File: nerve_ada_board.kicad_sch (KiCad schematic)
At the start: 64 parts, among them J10 CAN1, J11 CAN2, J2 TC2050-IDC, J3 2171750001, J5 WS2812B, J6 Camera, J7 PA4-7, J8 PC1-3, J9 PB4-5, SW1 SPST, SW2 SPST, SW3 SPST, U1 LD1117S33TR_SOT223, U2 STM32F446RET, U3 SAM-M10Q, U4 XBP9B-DMWT-002, U8 TXB0104QPWRQ1, U9 TXB0104QPWRQ1, Y1 8M, Y2 32k768

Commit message: Resolve ERC duplicate labelling warning
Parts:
- renumbered J8 to J10, J9 to J11, J10 to J7, J11 to J8, J7 to J9
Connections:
- net CAN1_HIGH+ renamed CAN1+
- net CAN1_LOW- renamed CAN1-
- net CAN2_HIGH+ renamed CAN2+
- net CAN2_LOW- renamed CAN2-
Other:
- moved on the sheet: J7, J8
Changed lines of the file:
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@@
 	(wire
 		(pts
-			(xy 262.89 163.83) (xy 271.78 163.83)
-		)
-		(stroke
-			(width 0)
-			(type default)
-		)
-	)
-	(wire
-		(pts
 			(xy 135.89 57.15) (xy 135.89 58.42)
 		)
@@
 	(wire
 		(pts
-			(xy 262.89 161.29) (xy 271.78 161.29)
-		)
-		(stroke
-			(width 0)
-			(type default)
-		)
-	)
-	(wire
-		(pts
 			(xy 167.64 121.92) (xy 167.64 123.19)
 		)
@@
 	(wire
 		(pts
-			(xy 205.74 161.29) (xy 214.63 161.29)
-		)
-		(stroke
-			(width 0)
-			(type default)
-		)
-	)
-	(wire
-		(pts
 			(xy 118.11 180.34) (xy 119.38 180.34)
 		)
@@
 	(wire
 		(pts
-			(xy 205.74 163.83) (xy 214.63 163.83)
-		)
-		(stroke
-			(width 0)
-			(type default)
-		)
-	)
-	(wire
-		(pts
 			(xy 85.09 180.34) (xy 86.36 180.34)
 		)
@@
 		)
 	)
-	(label "CAN2+"
-		(at 264.16 161.29 0)
-		(fields_autoplaced yes)
-		(effects
-			(font
-				(size 1.27 1.27)
-			)
-			(justify left bottom)
-		)
-	)
 	(label "LSE_OUT"
 		(at 58.42 118.11 180)
@@
 	)
 	(label "CAN1+"
-		(at 207.01 161.29 0)
-		(fields_autoplaced yes)
-		(effects
-			(font
-				(size 1.27 1.27)
-			)
-			(justify left bottom)
-		)
-	)
-	(label "CAN1+"
 		(at 205.74 152.4 0)
 		(fields_autoplaced yes)
@@
 		)
 	)
-	(label "CAN2-"
-		(at 264.16 163.83 0)
-		(fields_autoplaced yes)
-		(effects
-			(font
-				(size 1.27 1.27)
-			)
-			(justify left bottom)
-		)
-	)
-	(label "CAN1-"
-		(at 207.01 163.83 0)
-		(fields_autoplaced yes)
-		(effects
-			(font
-				(size 1.27 1.27)
-			)
-			(justify left bottom)
-		)
-	)
 	(hierarchical_label "SWO"
 		(shape input)
@@
 		)
 	)
-	(hierarchical_label "CAN1_LOW-"
-		(shape input)
-		(at 213.36 154.94 0)
-		(fields_autoplaced yes)
-		(effects
-			(font
-				(size 1.27 1.27)
-			)
-			(justify left)
-		)
-	)
 	(hierarchical_label "GPIO_IMU_P0"
 		(shape input)
@@
 		)
 	)
-	(hierarchical_label "CAN1_HIGH+"
-		(shape input)
-		(at 205.74 161.29 180)
-		(fields_autoplaced yes)
-		(effects
-			(font
-				(size 1.27 1.27)
-			)
-			(justify right)
-		)
-	)
 	(hierarchical_label "CAN2_RX"
 		(shape input)
@@
 		)
 	)
-	(hierarchical_label "CAN1_LOW-"
-		(shape input)
-		(at 205.74 163.83 180)
-		(fields_autoplaced yes)
-		(effects
-			(font
-				(size 1.27 1.27)
-			)
-			(justify right)
-		)
-	)
 	(hierarchical_label "PB5_EXP"
 		(shape input)
@@
 		)
 	)
-	(hierarchical_label "CAN2_HIGH+"
-		(shape input)
-		(at 270.51 152.4 0)
-		(fields_autoplaced yes)
-		(effects
-			(font
-				(size 1.27 1.27)
-			)
-			(justify left)
-		)
-	)
 	(hierarchical_label "PC2"
 		(shape input)
@@
 		)
 	)
-	(hierarchical_label "CAN1_HIGH+"
-		(shape input)
-		(at 213.36 152.4 0)
-		(fields_autoplaced yes)
-		(effects
-			(font
-				(size 1.27 1.27)
-			)
-			(justify left)
-		)
-	)
 	(hierarchical_label "USART2_RX"
 		(shape input)
@@
 		)
 	)
-	(hierarchical_label "CAN2_LOW-"
-		(shape input)
-		(at 270.51 154.94 0)
-		(fields_autoplaced yes)
-		(effects
-			(font
-				(size 1.27 1.27)
-			)
-			(justify left)
-		)
-	)
 	(hierarchical_label "GPIO_SPI2_CS"
 		(shape input)
@@
 		)
 	)
-	(hierarchical_label "CAN2_HIGH+"
-		(shape input)
-		(at 262.89 161.29 180)
-		(fields_autoplaced yes)
-		(effects
-			(font
-				(size 1.27 1.27)
-			)
-			(justify right)
-		)
-	)
 	(hierarchical_label "SDIO_DET"
 		(shape input)
@@
 		)
 	)
-	(hierarchical_label "CAN2_LOW-"
-		(shape input)
-		(at 262.89 163.83 180)
-		(fields_autoplaced yes)
-		(effects
-			(font
-				(size 1.27 1.27)
-			)
-			(justify right)
-		)
-	)
 	(hierarchical_label "CAN1_TX"
 		(shape input)
@@
 	(symbol
 		(lib_id "Connector:Conn_01x02_Pin")
-		(at 276.86 161.29 0)
+		(at 275.59 152.4 0)
 		(mirror y)
 		(unit 1)
@@
 		(on_board yes)
 		(dnp no)
-		(property "Reference" "J11"
-			(at 277.876 161.29 0)
+		(property "Reference" "J8"
+			(at 276.606 152.4 0)
 			(effects
 				(font
@@
 		)
 		(property "Value" "CAN2"
-			(at 277.876 163.83 0)
+			(at 276.606 154.94 0)
 			(effects
 				(font
@@
 		)
 		(property "Footprint" "Connector_PinHeader_2.54mm:PinHeader_1x02_P2.54mm_Vertical"
-			(at 276.86 161.29 0)
+			(at 275.59 152.4 0)
 			(effects
 				(font
@@
 		)
 		(property "Datasheet" "~"
-			(at 276.86 161.29 0)
+			(at 275.59 152.4 0)
 			(effects
 				(font
@@
 		)
 		(property "Description" "Generic connector, single row, 01x02, script generated"
-			(at 276.86 161.29 0)
+			(at 275.59 152.4 0)
 			(effects
 				(font
@@
 			(project ""
 				(path "/c0277862-b3f2-4e0e-986f-34702f0543f0"
-					(reference "J11")
+					(reference "J8")
 					(unit 1)
 				)
@@
 		(dnp no)
 		(fields_autoplaced yes)
-		(property "Reference" "J8"
+		(property "Reference" "J10"
 			(at 67.31 154.9399 0)
 			(effects
@@
 			(project ""
 				(path "/c0277862-b3f2-4e0e-986f-34702f0543f0"
-					(reference "J8")
+					(reference "J10")
 					(unit 1)
 				)
@@
 		(on_board yes)
 		(dnp no)
-		(property "Reference" "J7"
+		(property "Reference" "J9"
 			(at 28.956 154.686 0)
 			(effects
@@
 			(project "nerve_ada_board"
 				(path "/c0277862-b3f2-4e0e-986f-34702f0543f0"
-					(reference "J7")
+					(reference "J9")
 					(unit 1)
 				)
@@
 	(symbol
 		(lib_id "Connector:Conn_01x02_Pin")
-		(at 219.71 161.29 0)
+		(at 218.44 152.4 0)
 		(mirror y)
 		(unit 1)
@@
 		(on_board yes)
 		(dnp no)
-		(property "Reference" "J10"
-			(at 220.726 161.29 0)
+		(property "Reference" "J7"
+			(at 219.456 152.4 0)
 			(effects
 				(font
@@
 		)
 		(property "Value" "CAN1"
-			(at 220.726 163.83 0)
+			(at 219.456 154.94 0)
 			(effects
 				(font
@@
 		)
 		(property "Footprint" "Connector_PinHeader_2.54mm:PinHeader_1x02_P2.54mm_Vertical"
-			(at 219.71 161.29 0)
+			(at 218.44 152.4 0)
 			(effects
 				(font
@@
 		)
 		(property "Datasheet" "~"
-			(at 219.71 161.29 0)
+			(at 218.44 152.4 0)
 			(effects
 				(font
@@
 		)
 		(property "Description" "Generic connector, single row, 01x02, script generated"
-			(at 219.71 161.29 0)
+			(at 218.44 152.4 0)
 			(effects
 				(font
@@
 			(project "nerve_ada_board"
 				(path "/c0277862-b3f2-4e0e-986f-34702f0543f0"
-					(reference "J10")
+					(reference "J7")
 					(unit 1)
 				)
@@
 		(on_board yes)
 		(dnp no)
-		(property "Reference" "J9"
+		(property "Reference" "J11"
 			(at 96.52 156.21 0)
 			(effects
@@
 			(project "nerve_ada_board"
 				(path "/c0277862-b3f2-4e0e-986f-34702f0543f0"
-					(reference "J9")
+					(reference "J11")
 					(unit 1)
 				)

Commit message: Flight ready alpha and update components
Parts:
- removed J1: ~, adafruit:adafruit_4682_sdio_card, symbol adafruit:adafruit_4682_sdio_card
- removed J12, J13, J14, J15, J16, J17, J18: ~, common:harwin_2p_2-54_jumper_closed, symbol common:harwin_2p_2-54_jumper_closed
- removed J5: WS2812B, Connector_PinHeader_2.54mm:PinHeader_1x03_P2.54mm_Vertical, symbol Connector:Conn_01x03_Pin
- added J1: ~, common:harwin_2p_2-54_jumper_open, symbol common:harwin_2p_2-54_jumper_open
- added J3: 472192001, common:molex_472192001_microsd_hinge, symbol common:molex_472192001_microsd_hinge
- added J6: WS2812B, Connector_PinHeader_2.54mm:PinHeader_1x02_P2.54mm_Vertical, symbol Connector:Conn_01x02_Pin
- added R1, R2, R3, R4, R5: 47k, Resistor_SMD:R_0603_1608Metric, symbol Device:R
- added R6: 10k, Resistor_SMD:R_0603_1608Metric, symbol Device:R
- renumbered J6 to J12, J3 to J4, J4 to J5, R4 to R10, R5 to R11, R6 to R12, R7 to R13, R8 to R14, R1 to R7, R2 to R8, R3 to R9, U9 to U10, U10 to U3, U3 to U4, U4 to U5, U5 to U6, U6 to U7, U7 to U8, U8 to U9
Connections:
- net +3V3: now also J1.1, J3.4 (VDD), R1.1, R2.1, R3.1, R4.1, R5.1
- net GND: now also J3.6 (VSS), J3.G1 (GND), J3.G2 (GND), J3.G3 (GND), J3.G4 (GND), J6.1 (Pin_1), R6.2
- net PB4: now also U9.4 (A3)
- net PB5: now also U9.5 (A4)
- net PC1: now also U10.2 (A1)
- net PC2: now also U10.3 (A2)
- net PC3: now also U10.4 (A3)
- net SDIO_CLK: now also J3.5 (CLK)
- net SDIO_CMD: now also J3.3 (CMD), R3.2
- net SDIO_D0: now also J3.7 (DAT0), R2.2
- net SDIO_D1: now also J3.8 (DAT1), R1.2
- net SDIO_D2: now also J3.1 (DAT2), R5.2
- net SDIO_D3: now also J3.2 (DAT3/CD), R4.2
- net SDIO_DET: now also J1.2, R6.1
- net USART3_RX: now also U9.2 (A1)
- net USART3_TX: now also U9.3 (A2)
- net at D4.2 (DOUT): now also J6.2 (Pin_2)
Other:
- note added: "Manual card detect jumper."
- moved on the sheet: BT1, C6, C7, D1, D2, D3, D4, J10, J11, J12, J7, J8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

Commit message: Fix SDIO card detect for active low
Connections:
- net +3V3: now also R6.1; no longer J1.1
- net GND: now also J1.2; no longer R6.2
- net SDIO_DET: now also J1.1, R6.2; no longer J1.2, R6.1
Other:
- moved on the sheet: J1
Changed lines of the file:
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@@
 	)
 	(junction
-		(at 154.94 24.13)
+		(at 252.73 19.05)
 		(diameter 0)
 		(color 0 0 0 0)
 	)
 	(junction
-		(at 252.73 19.05)
+		(at 181.61 85.09)
 		(diameter 0)
 		(color 0 0 0 0)
 	)
 	(junction
-		(at 181.61 85.09)
+		(at 142.24 27.94)
 		(diameter 0)
 		(color 0 0 0 0)
@@
 	(wire
 		(pts
-			(xy 154.94 21.59) (xy 153.67 21.59)
-		)
-		(stroke
-			(width 0)
-			(type default)
-		)
-	)
-	(wire
-		(pts
 			(xy 93.98 118.11) (xy 95.25 118.11)
 		)
@@
 	(wire
 		(pts
-			(xy 154.94 24.13) (xy 153.67 24.13)
+			(xy 153.67 35.56) (xy 154.94 35.56)
 		)
 		(stroke
@@
 	(wire
 		(pts
-			(xy 154.94 25.4) (xy 154.94 24.13)
-		)
-		(stroke
-			(width 0)
-			(type default)
-		)
-	)
-	(wire
-		(pts
 			(xy 245.11 64.77) (xy 245.11 80.01)
 		)
@@
 	(wire
 		(pts
-			(xy 154.94 24.13) (xy 154.94 21.59)
-		)
-		(stroke
-			(width 0)
-			(type default)
-		)
-	)
-	(wire
-		(pts
 			(xy 171.45 121.92) (xy 171.45 123.19)
 		)
@@
 	(wire
 		(pts
+			(xy 142.24 19.05) (xy 142.24 17.78)
+		)
+		(stroke
+			(width 0)
+			(type default)
+		)
+	)
+	(wire
+		(pts
 			(xy 73.66 34.29) (xy 73.66 50.8)
 		)
@@
 	(wire
 		(pts
+			(xy 142.24 27.94) (xy 142.24 26.67)
+		)
+		(stroke
+			(width 0)
+			(type default)
+		)
+	)
+	(wire
+		(pts
 			(xy 31.75 102.87) (xy 31.75 104.14)
 		)
@@
 	(wire
 		(pts
-			(xy 142.24 21.59) (xy 142.24 17.78)
+			(xy 142.24 35.56) (xy 142.24 27.94)
 		)
 		(stroke
@@
 	(wire
 		(pts
-			(xy 154.94 33.02) (xy 154.94 34.29)
+			(xy 144.78 27.94) (xy 142.24 27.94)
+		)
+		(stroke
+			(width 0)
+			(type default)
+		)
+	)
+	(wire
+		(pts
+			(xy 154.94 35.56) (xy 154.94 36.83)
 		)
 		(stroke
@@
 	(wire
 		(pts
-			(xy 143.51 21.59) (xy 142.24 21.59)
+			(xy 143.51 35.56) (xy 142.24 35.56)
 		)
 		(stroke
@@
 		)
 	)
+	(hierarchical_label "SDIO_DET"
+		(shape input)
+		(at 144.78 27.94 0)
+		(fields_autoplaced yes)
+		(effects
+			(font
+				(size 1.27 1.27)
+			)
+			(justify left)
+		)
+	)
 	(hierarchical_label "USART1_RTS"
 		(shape input)
@@
 		)
 	)
-	(hierarchical_label "SDIO_DET"
-		(shape input)
-		(at 153.67 24.13 180)
-		(fields_autoplaced yes)
-		(effects
-			(font
-				(size 1.27 1.27)
-			)
-			(justify right)
-		)
-	)
 	(hierarchical_label "PC1_EXP"
 		(shape input)
@@
 	)
 	(symbol
+		(lib_id "Device:R")
+		(at 142.24 22.86 0)
+		(unit 1)
+		(exclude_from_sim no)
+		(in_bom yes)
+		(on_board yes)
+		(dnp no)
+		(property "Reference" "R6"
+			(at 138.176 21.59 0)
+			(effects
+				(font
+					(size 1.27 1.27)
+				)
+				(justify left)
+			)
+		)
+		(property "Value" "10k"
+			(at 137.16 24.13 0)
+			(effects
+				(font
+					(size 1.27 1.27)
+				)
+				(justify left)
+			)
+		)
+		(property "Footprint" "Resistor_SMD:R_0603_1608Metric"
+			(at 140.462 22.86 90)
+			(effects
+				(font
+					(size 1.27 1.27)
+				)
+				(hide yes)
+			)
+		)
+		(property "Datasheet" "~"
+			(at 142.24 22.86 0)
+			(effects
+				(font
+					(size 1.27 1.27)
+				)
+				(hide yes)
+			)
+		)
+		(property "Description" "Resistor"
+			(at 142.24 22.86 0)
+			(effects
+				(font
+					(size 1.27 1.27)
+				)
+				(hide yes)
+			)
+		)
+		(pin "2"
+		)
+		(pin "1"
+		)
+		(instances
+			(project "nerve_ada_board"
+				(path "/c0277862-b3f2-4e0e-986f-34702f0543f0"
+					(reference "R6")
+					(unit 1)
+				)
+			)
+		)
+	)
+	(symbol
 		(lib_id "power:GND")
-		(at 154.94 34.29 0)
+		(at 154.94 36.83 0)
 		(unit 1)
 		(exclude_from_sim no)
@@
 		(fields_autoplaced yes)
 		(property "Reference" "#PWR010"
-			(at 154.94 40.64 0)
+			(at 154.94 43.18 0)
 			(effects
 				(font
@@
 		)
 		(property "Value" "GND"
-			(at 154.94 39.37 0)
+			(at 154.94 41.91 0)
 			(effects
 				(font
@@
 		)
 		(property "Footprint" ""
-			(at 154.94 34.29 0)
+			(at 154.94 36.83 0)
 			(effects
 				(font
@@
 		)
 		(property "Datasheet" ""
-			(at 154.94 34.29 0)
+			(at 154.94 36.83 0)
 			(effects
 				(font
@@
 		)
 		(property "Description" "Power symbol creates a global label with name \"GND\" , ground"
-			(at 154.94 34.29 0)
+			(at 154.94 36.83 0)
 			(effects
 				(font
@@
 	)
 	(symbol
-		(lib_id "Device:R")
-		(at 154.94 29.21 0)
-		(unit 1)
-		(exclude_from_sim no)
-		(in_bom yes)
-		(on_board yes)
-		(dnp no)
-		(property "Reference" "R6"
-			(at 150.876 27.94 0)
-			(effects
-				(font
-					(size 1.27 1.27)
-				)
-				(justify left)
-			)
-		)
-		(property "Value" "10k"
-			(at 149.86 30.48 0)
-			(effects
-				(font
-					(size 1.27 1.27)
-				)
-				(justify left)
-			)
-		)
-		(property "Footprint" "Resistor_SMD:R_0603_1608Metric"
-			(at 153.162 29.21 90)
-			(effects
-				(font
-					(size 1.27 1.27)
-				)
-				(hide yes)
-			)
-		)
-		(property "Datasheet" "~"
-			(at 154.94 29.21 0)
-			(effects
-				(font
-					(size 1.27 1.27)
-				)
-				(hide yes)
-			)
-		)
-		(property "Description" "Resistor"
-			(at 154.94 29.21 0)
-			(effects
-				(font
-					(size 1.27 1.27)
-				)
-				(hide yes)
-			)
-		)
-		(pin "2"
-		)
-		(pin "1"
-		)
-		(instances
-			(project "nerve_ada_board"
-				(path "/c0277862-b3f2-4e0e-986f-34702f0543f0"
-					(reference "R6")
-					(unit 1)
-				)
-			)
-		)
-	)
-	(symbol
 		(lib_id "power:+3V3")
 		(at 16.51 17.78 0)
@@
 	(symbol
 		(lib_id "common:harwin_2p_2-54_jumper_open")
-		(at 148.59 21.59 0)
+		(at 148.59 35.56 0)
 		(unit 1)
 		(exclude_from_sim no)
@@
 		(dnp no)
 		(property "Reference" "J1"
-			(at 148.59 18.288 0)
+			(at 148.59 32.258 0)
 			(effects
 				(font
@@
 		)
 		(property "Value" "~"
-			(at 148.59 17.78 0)
+			(at 148.59 31.75 0)
 			(effects
 				(font
@@
 		)
 		(property "Footprint" "common:harwin_2p_2-54_jumper_open"
-			(at 152.4 27.94 0)
+			(at 152.4 41.91 0)
 			(effects
 				(font
@@
 		)
 		(property "Datasheet" "https://cdn.harwin.com/pdfs/M20-999.pdf"
-			(at 184.15 29.083 0)
+			(at 184.15 43.053 0)
 			(effects
 				(font
@@
 		)
 		(property "Description" "Connector Header Through Hole 2 position 0.100\" (2.54mm)"
-			(at 184.15 29.083 0)
+			(at 184.15 43.053 0)
 			(effects
 				(font
@@
 		)
 		(property "Manufacturer" "Harwin"
-			(at 184.15 20.193 0)
+			(at 184.15 34.163 0)
 			(effects
 				(font
@@
 		)
 		(property "Manufacturer Part Number" "M20-9990246"
-			(at 184.15 20.193 0)
+			(at 184.15 34.163 0)
 			(effects
 				(font
@@
 		)
 		(property "Distributor" "DigiKey"
-			(at 184.15 20.193 0)
+			(at 184.15 34.163 0)
 			(effects
 				(font
@@
 		)
 		(property "Distributor Part Number" "952-2262-ND"
-			(at 184.15 29.083 0)
+			(at 184.15 43.053 0)
 			(effects
 				(font
@@
 		)
 		(property "Distributor Link" "https://www.digikey.ca/en/products/detail/harwin-inc/M20-9990246/3728226"
-			(at 184.15 29.083 0)
+			(at 184.15 43.053 0)
 			(effects
 				(font

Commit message: Swap to LD39150DT33-R regulator
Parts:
- removed U1: LD1117S33TR_SOT223, Package_TO_SOT_SMD:SOT-223-3_TabPin2, symbol Regulator_Linear:LD1117S33TR_SOT223
- added U1: ld39150dt33-r, common:to-252-2_dpak-2-leg, symbol common:ld39150dt33-r
- C8: value 100n -> 1u
- C9: value 10u -> 2u2; footprint Capacitor_SMD:C_0805_2012Metric -> Capacitor_SMD:C_0603_1608Metric
- renumbered J2 to J1, J3 to J2, J4 to J3, J1 to J4
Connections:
- net +3V3: now also U1.3 (VO)
- net +5V: now also U1.1 (VI)
- net GND: now also U1.2 (GND)
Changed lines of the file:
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@@
 			)
 		)
-		(property "Value" "10u"
+		(property "Value" "2u2"
 			(at 280.67 31.75 0)
 			(effects
@@
 			)
 		)
-		(property "Footprint" "Capacitor_SMD:C_0805_2012Metric"
+		(property "Footprint" "Capacitor_SMD:C_0603_1608Metric"
 			(at 279.0952 34.29 0)
 			(effects
@@
 			)
 		)
-		(property "Value" "100n"
+		(property "Value" "1u"
 			(at 255.27 31.75 0)
 			(effects
@@
 		(on_board yes)
 		(dnp no)
-		(property "Reference" "J3"
+		(property "Reference" "J2"
 			(at 194.056 45.974 0)
 			(effects
@@
 			(project ""
 				(path "/c0277862-b3f2-4e0e-986f-34702f0543f0"
-					(reference "J3")
+					(reference "J2")
 					(unit 1)
 				)
@@
 	)
 	(symbol
-		(lib_id "Regulator_Linear:LD1117S33TR_SOT223")
-		(at 265.43 25.4 0)
-		(unit 1)
-		(exclude_from_sim no)
-		(in_bom yes)
-		(on_board yes)
-		(dnp no)
-		(property "Reference" "U1"
-			(at 265.43 19.304 0)
-			(effects
-				(font
-					(size 1.27 1.27)
-				)
-			)
-		)
-		(property "Value" "LD1117S33TR_SOT223"
-			(at 265.43 21.844 0)
-			(effects
-				(font
-					(size 1.27 1.27)
-				)
-			)
-		)
-		(property "Footprint" "Package_TO_SOT_SMD:SOT-223-3_TabPin2"
-			(at 265.43 20.32 0)
-			(effects
-				(font
-					(size 1.27 1.27)
-				)
-				(hide yes)
-			)
-		)
-		(property "Datasheet" "http://www.st.com/st-web-ui/static/active/en/resource/technical/document/datasheet/CD00000544.pdf"
-			(at 267.97 31.75 0)
-			(effects
-				(font
-					(size 1.27 1.27)
-				)
-				(hide yes)
-			)
-		)
-		(property "Description" "800mA Fixed Low Drop Positive Voltage Regulator, Fixed Output 3.3V, SOT-223"
-			(at 265.43 25.4 0)
-			(effects
-				(font
-					(size 1.27 1.27)
-				)
-				(hide yes)
-			)
-		)
-		(pin "2"
-		)
-		(pin "3"
-		)
-		(pin "1"
-		)
-		(instances
-			(project ""
-				(path "/c0277862-b3f2-4e0e-986f-34702f0543f0"
-					(reference "U1")
-					(unit 1)
-				)
-			)
-		)
-	)
-	(symbol
 		(lib_id "Device:R")
 		(at 107.95 48.26 0)
@@
 		(on_board yes)
 		(dnp no)
-		(property "Reference" "J4"
+		(property "Reference" "J3"
 			(at 231.14 16.256 0)
 			(effects
@@
 			(project ""
 				(path "/c0277862-b3f2-4e0e-986f-34702f0543f0"
-					(reference "J4")
+					(reference "J3")
 					(unit 1)
 				)
@@
 		(dnp no)
 		(fields_autoplaced yes)
-		(property "Reference" "#PWR010"
+		(property "Reference" "#PWR011"
 			(at 154.94 43.18 0)
 			(effects
@@
 			(project "nerve_ada_board"
 				(path "/c0277862-b3f2-4e0e-986f-34702f0543f0"
-					(reference "#PWR010")
+					(reference "#PWR011")
 					(unit 1)
 				)
@@
 		(dnp no)
 		(fields_autoplaced yes)
-		(property "Reference" "#PWR011"
+		(property "Reference" "#PWR010"
 			(at 129.54 43.18 0)
 			(effects
@@
 			(project "nerve_ada_board"
 				(path "/c0277862-b3f2-4e0e-986f-34702f0543f0"
-					(reference "#PWR011")
+					(reference "#PWR010")
 					(unit 1)
 				)
@@
 		(on_board yes)
 		(dnp no)
-		(property "Reference" "J1"
+		(property "Reference" "J4"
 			(at 148.59 32.258 0)
 			(effects
@@
 			(project "nerve_ada_board"
 				(path "/c0277862-b3f2-4e0e-986f-34702f0543f0"
-					(reference "J1")
+					(reference "J4")
 					(unit 1)
 				)
@@
 		(on_board yes)
 		(dnp no)
-		(property "Reference" "J2"
+		(property "Reference" "J1"
 			(at 20.32 17.78 0)
 			(effects
@@
 			(project ""
 				(path "/c0277862-b3f2-4e0e-986f-34702f0543f0"
-					(reference "J2")
+					(reference "J1")
 					(unit 1)
 				)
@@
 					(unit 1)
 				)
+			)
+		)
+	)
+	(symbol
+		(lib_id "common:ld39150dt33-r")
+		(at 265.43 25.4 0)
+		(unit 1)
+		(exclude_from_sim no)
+		(in_bom yes)
+		(on_board yes)
+		(dnp no)
+		(property "Reference" "U1"
+			(at 265.43 19.05 0)
+			(effects
+				(font
+					(size 1.27 1.27)
+				)
+			)
+		)
+		(property "Value" "ld39150dt33-r"
+			(at 265.43 21.59 0)
+			(effects
+				(font
+					(size 1.27 1.27)
+				)
+			)
+		)
+		(property "Footprint" "common:to-252-2_dpak-2-leg"
+			(at 265.43 20.32 0)
+			(effects
+				(font
+					(size 1.27 1.27)
+				)
+				(hide yes)
+			)
+		)
+		(property "Datasheet" "https://www.st.com/resource/en/datasheet/ld39150.pdf"
+			(at 267.97 31.75 0)
+			(effects
+				(font
+					(size 1.27 1.27)
+				)
+				(hide yes)
+			)
+		)
+		(property "Description" "1.5A Ultra Low Dropout regulator, positive, 3.3V fixed output, TO-252"
+			(at 265.43 25.4 0)
+			(effects
+				(font
+					(size 1.27 1.27)
+				)
+				(hide yes)
+			)
+		)
+		(property "Manufacturer" "STMicroelectronics"
+			(at 265.43 25.4 0)
+			(effects
+				(font
+					(size 1.27 1.27)
+				)
+				(hide yes)
+			)
+		)
+		(property "Manufacturer Part Number" "LD39150DT33-R"
+			(at 265.43 25.4 0)
+			(effects
+				(font
+					(size 1.27 1.27)
+				)
+				(hide yes)
+			)
+		)
+		(property "Distributor" "DigiKey"
+			(at 265.43 25.4 0)
+			(effects
+				(font
+					(size 1.27 1.27)
+				)
+				(hide yes)
+			)
+		)
+		(property "Distributor Part Number" "497-6448-1-ND"
+			(at 265.43 25.4 0)
+			(effects
+				(font
+					(size 1.27 1.27)
+				)
+				(hide yes)
+			)
+		)
+		(property "Distributor Link" "https://www.digikey.ca/en/products/detail/stmicroelectronics/LD39150DT33-R/1657323"
+			(at 265.43 25.4 0)
+			(effects
+				(font
+					(size 1.27 1.27)
+				)
+				(hide yes)
+			)
+		)
+		(pin "2"
+		)
+		(pin "1"
+		)
+		(pin "3"
+		)
+		(instances
+			(project ""
+				(path "/c0277862-b3f2-4e0e-986f-34702f0543f0"
+					(reference "U1")
+					(unit 1)
+				)

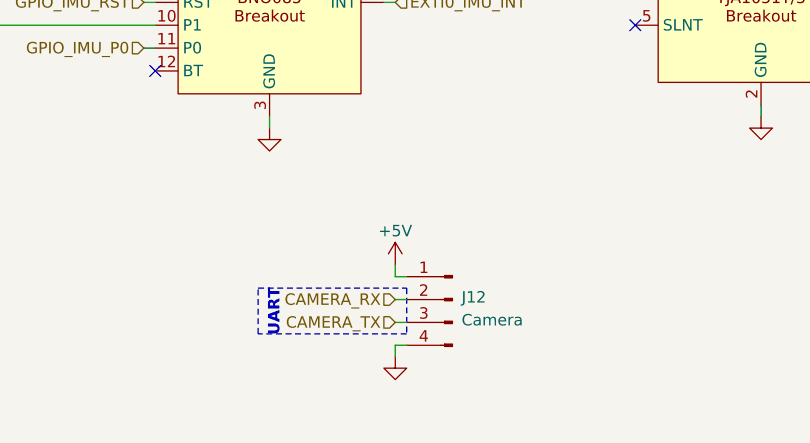
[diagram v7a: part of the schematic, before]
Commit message: Add mounting holes and cleanup layout
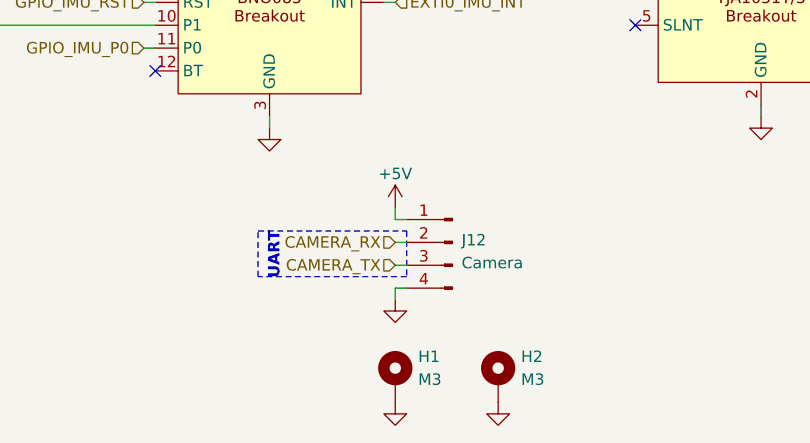
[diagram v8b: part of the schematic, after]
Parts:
- added H1, H2: M3, MountingHole:MountingHole_3.2mm_M3_Pad_Via, symbol Mechanical:MountingHole_Pad
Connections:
- net GND: now also H1.1, H2.1
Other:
- moved on the sheet: J12
